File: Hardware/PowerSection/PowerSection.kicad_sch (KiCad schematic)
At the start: 39 parts, among them J1 JST-B5B-XH-A, J2 Conn_01x02_Pin, Q1 2N7002, Q2 CMD05N03A, U1 INA180B4, U2 INA180B1, U4 ZXGD3009DY

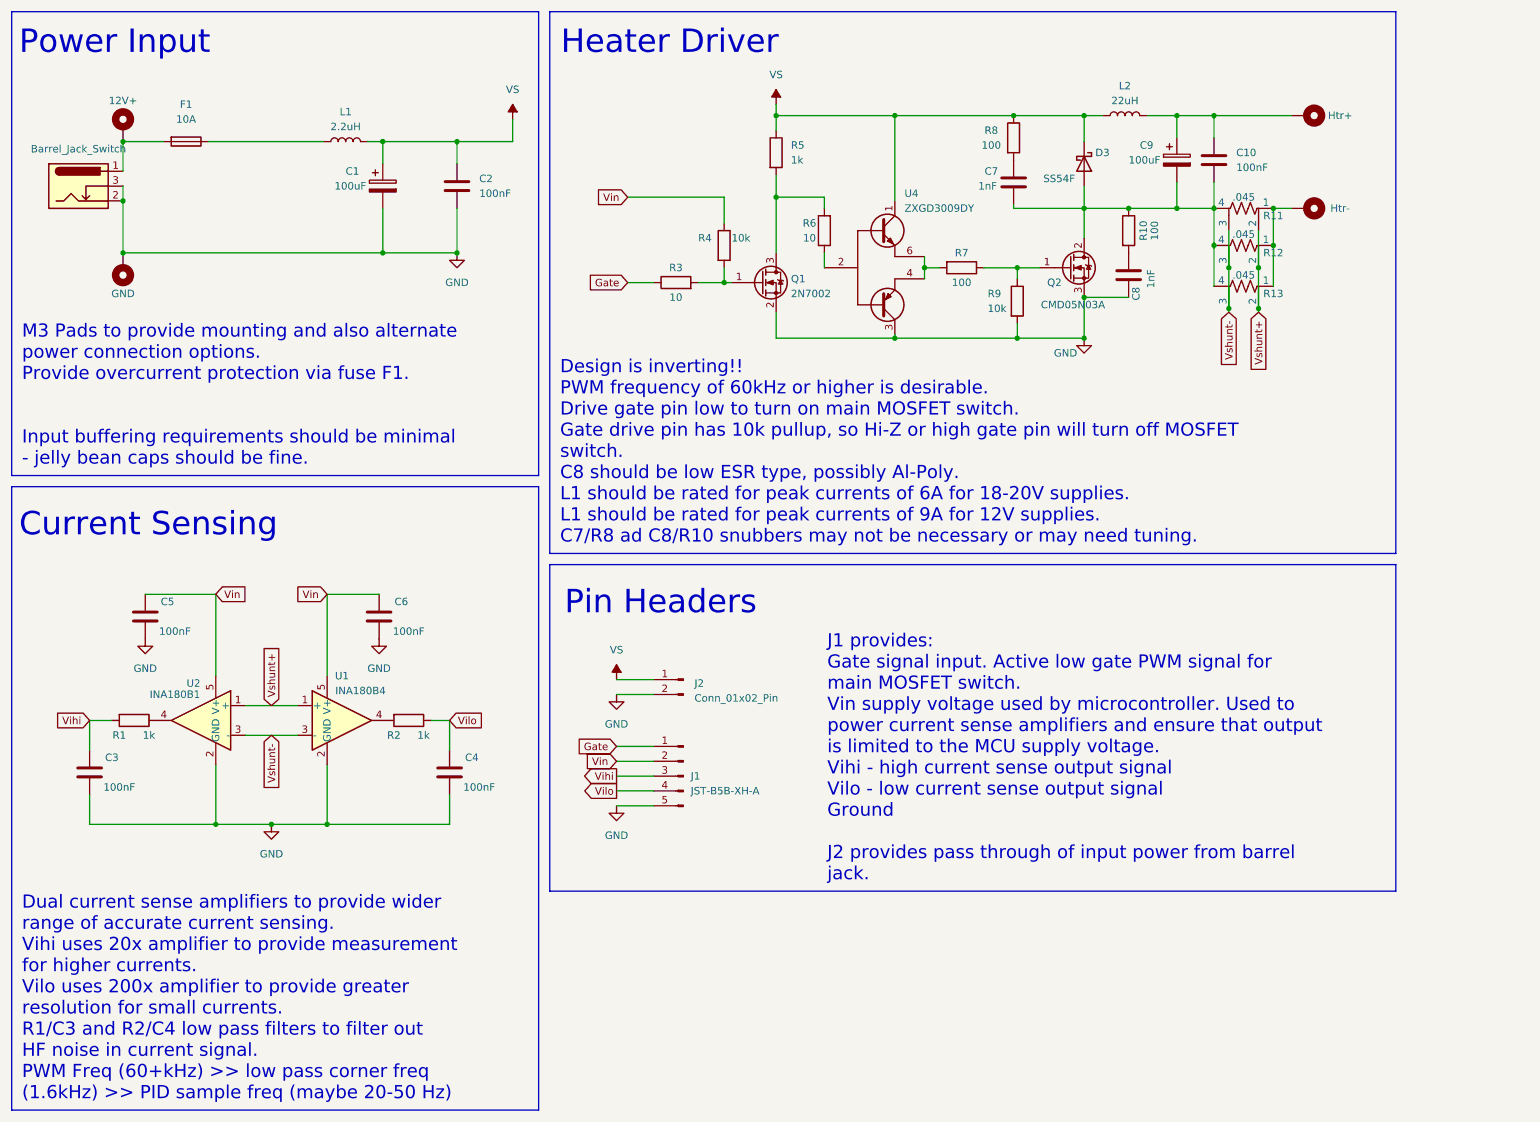
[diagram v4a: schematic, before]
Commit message: Initial rough layout completed, with minor schematic changes to address layout challenges.
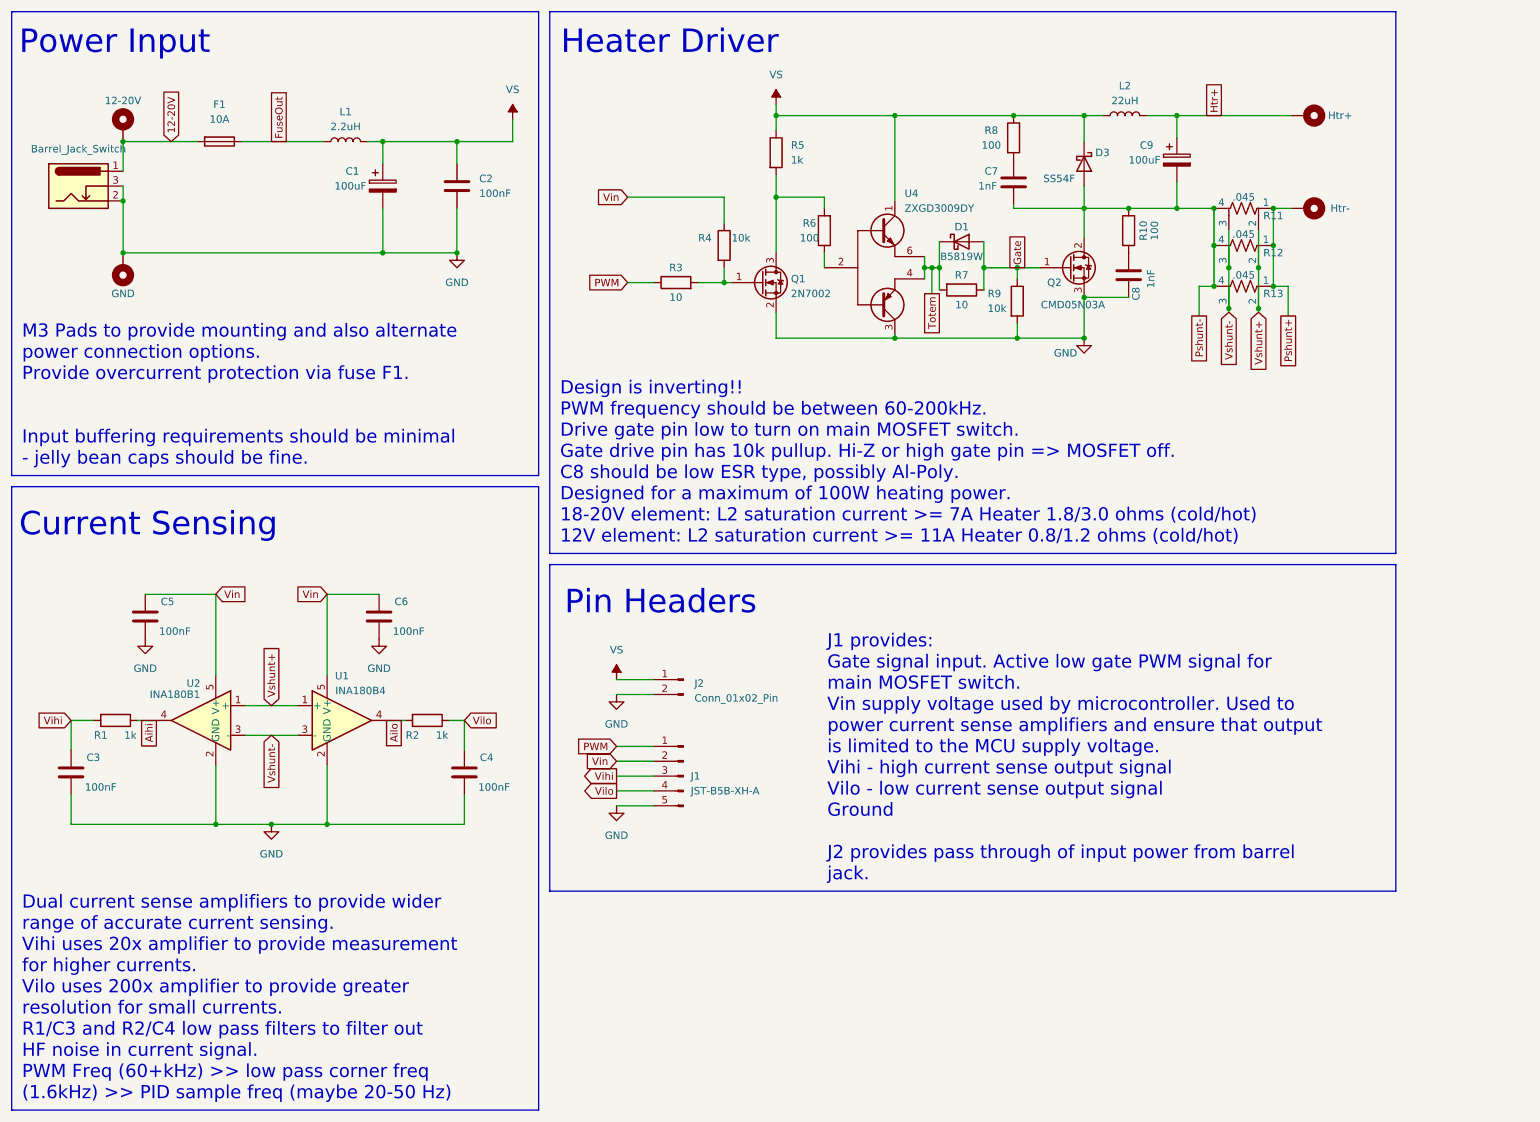
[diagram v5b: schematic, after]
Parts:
- removed C10: 100nF, Capacitor_SMD:C_0603_1608Metric, symbol Device:C
- added D1: B5819W, Diode_SMD:D_SOD-123, symbol Diode:B130-E3
- C7: footprint Capacitor_SMD:C_0603_1608Metric -> Resistor_SMD:R_0603_1608Metric
- H1: renamed from H2; footprint (none) -> MountingHole:MountingHole_3.2mm_M3_Pad_Via; Name 12V+ -> 12-20V
- H2: renamed from H5; footprint (none) -> MountingHole:MountingHole_3.2mm_M3_Pad_Via
- R6: value 10 -> 100
- R7: value 100 -> 10
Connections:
- net Gate: now also Q2.1 (G), R7.1, R9.1, D1.2 (A); no longer J1.1 (Pin_1), R3.1
- net Pshunt-: now reaches C7.2, C9.2, D3.2 (A), Q2.2 (D), R10.1, R11.4, R12.4, R13.4
- net Pshunt+: now reaches H4.1, R11.1, R12.1, R13.1
- net Htr+: now reaches C9.1, H3.1, L2.2
- net FuseOut: now reaches F1.1, L1.1
- net Aihi: now reaches R1.1, U2.4
- net Totem: now reaches R7.2, U4.4 (Sink), U4.6 (Source)
- net Totem: now also D1.1 (K)
- net 12-20V: now reaches 12V1.1, F1.2, H1.1
- net Ailo: now reaches R2.2, U1.4
- new net PWM: J1.1 (Pin_1), R3.1
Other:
- moved on the sheet: C3, C4, F1, R1, R2, R7
